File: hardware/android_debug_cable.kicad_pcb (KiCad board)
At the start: 2 copper layers, 25.5 x 10.5 mm, 11 parts, among them P1 USB_OTG, P2 50-00397, P3 CONN_01X04, U1 TCR2EF18, U2 CP2102N-A01-GQFN24

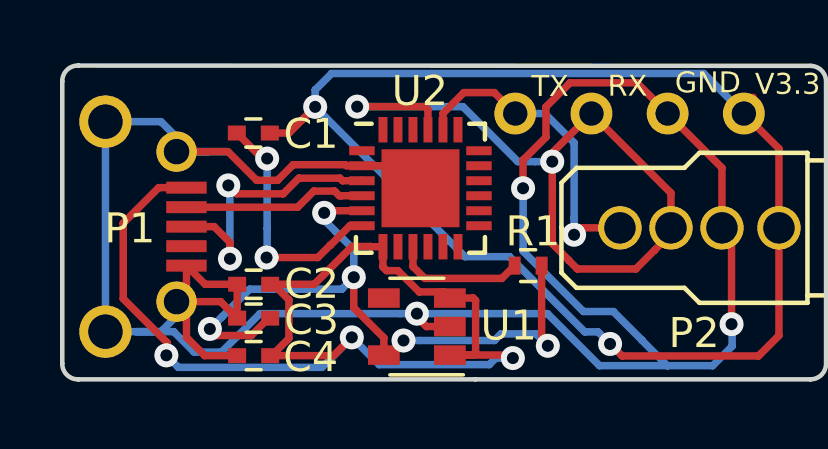
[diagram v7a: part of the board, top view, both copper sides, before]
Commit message: Move logo/version number around
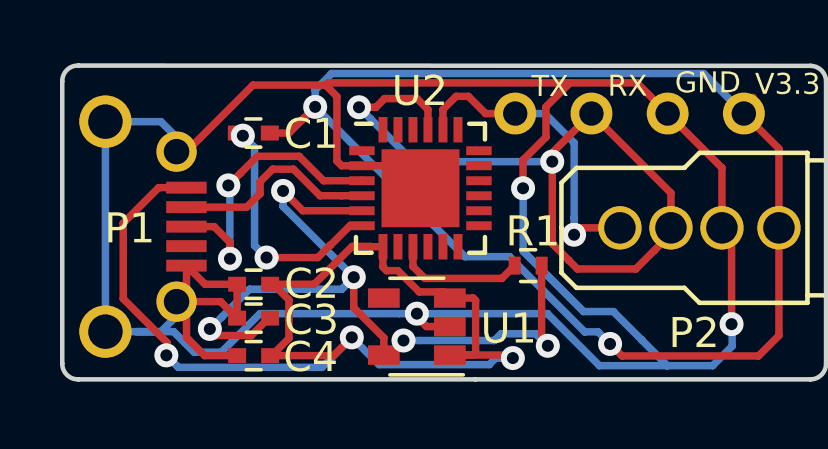
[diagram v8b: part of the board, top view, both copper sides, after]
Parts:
- moved G*** 0.15 mm to (139.6, 88.7)
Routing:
- net GND: track 85.5 -> 94.1 mm
- net V1.8: track 23.4 -> 26.3 mm
- net USB_D-: track 6.14 -> 6.97 mm
